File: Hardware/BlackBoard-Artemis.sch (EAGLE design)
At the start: 84 parts, among them IC3 LM1117, J2 CORTEX_DEBUG, J3 POWER_JACKTOE, J5 USB-C, Q1 1.1A/60V/600mΩ, U3 AP2112-3.3V, U4 ARTEMIS_MODULESMD, U5 CH340C, Y1 32.768kHz

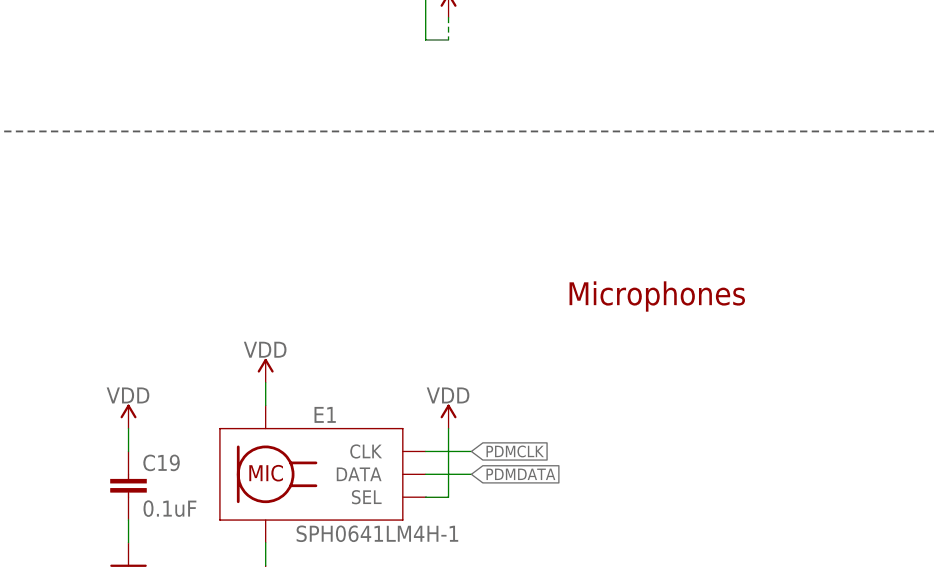
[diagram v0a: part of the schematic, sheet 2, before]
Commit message: Adding production panel
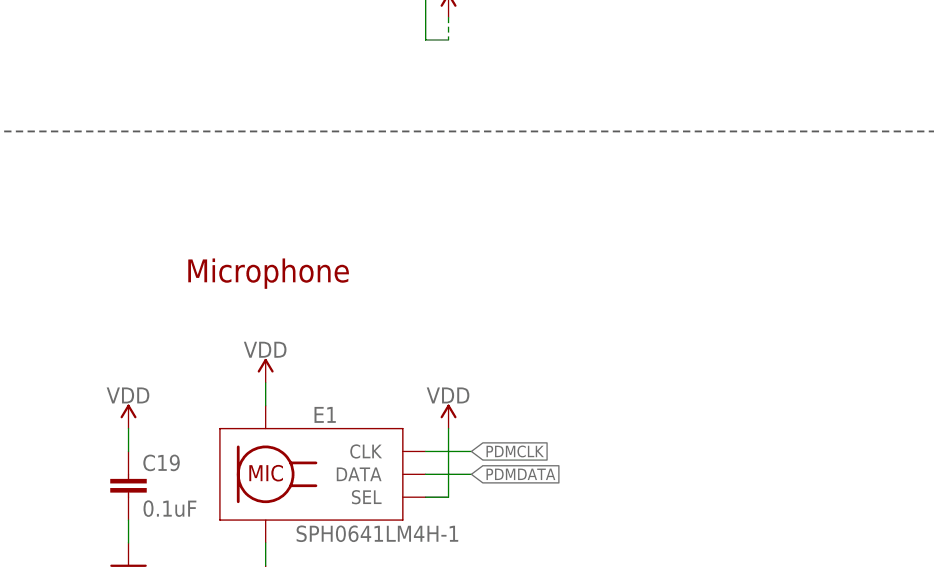
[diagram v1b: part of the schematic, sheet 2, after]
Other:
- note added: "Microphone"
- note removed: "Microphones"
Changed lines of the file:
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@@
 current measurements</text>
 <text x="122.174" y="180.086" size="2.54" layer="94" font="vector" ratio="15" align="center">Power Supplies</text>
-<text x="78.994" y="78.486" size="2.54" layer="94" font="vector" ratio="15" align="center">Microphones</text>
+<text x="35.814" y="81.026" size="2.54" layer="94" font="vector" ratio="15" align="center">Microphone</text>
 <wire x1="0" y1="96.52" x2="147.32" y2="96.52" width="0.2032" layer="97" style="longdash"/>
 <wire x1="147.32" y1="96.52" x2="248.92" y2="96.52" width="0.2032" layer="97" style="longdash"/>

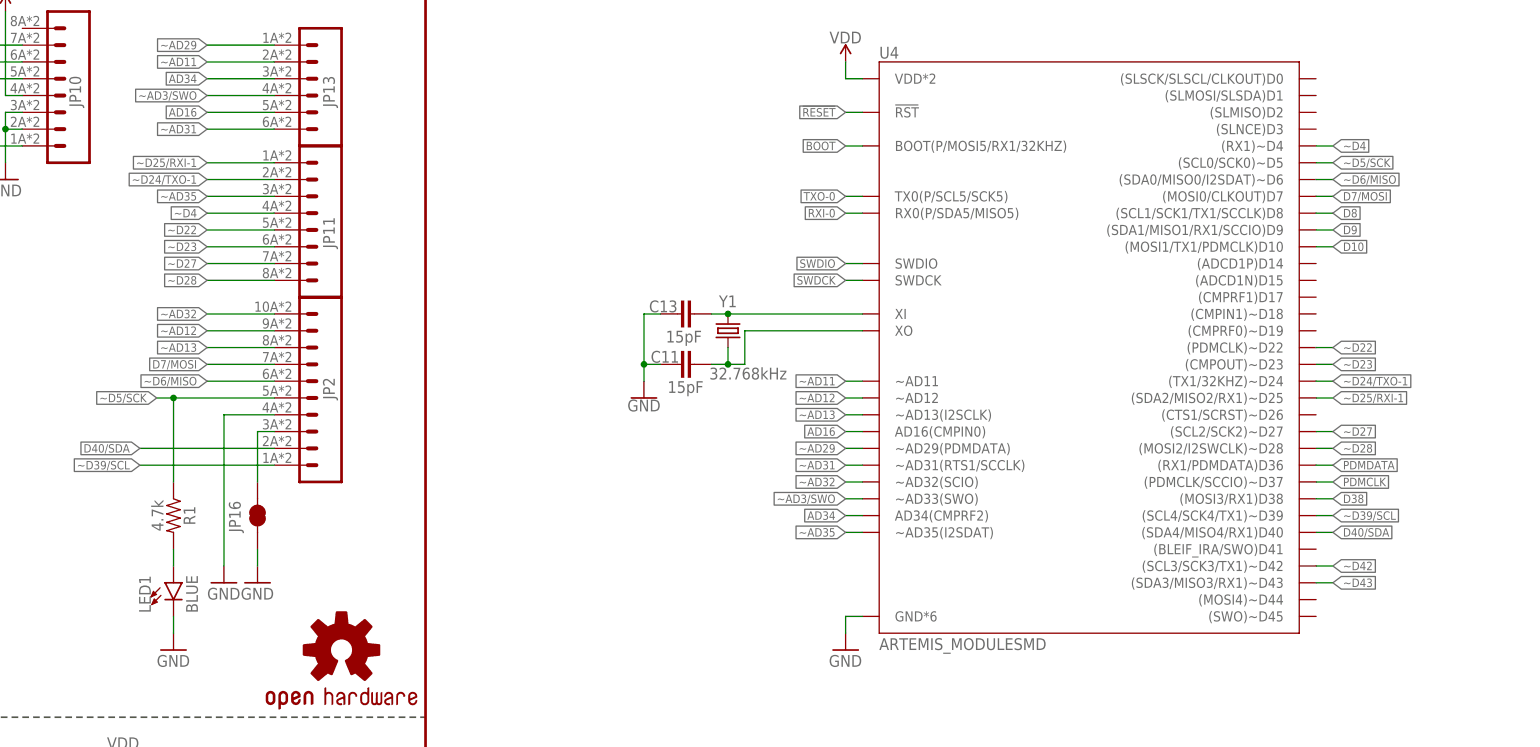
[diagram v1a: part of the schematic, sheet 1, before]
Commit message: Fixing PWM on pin 7
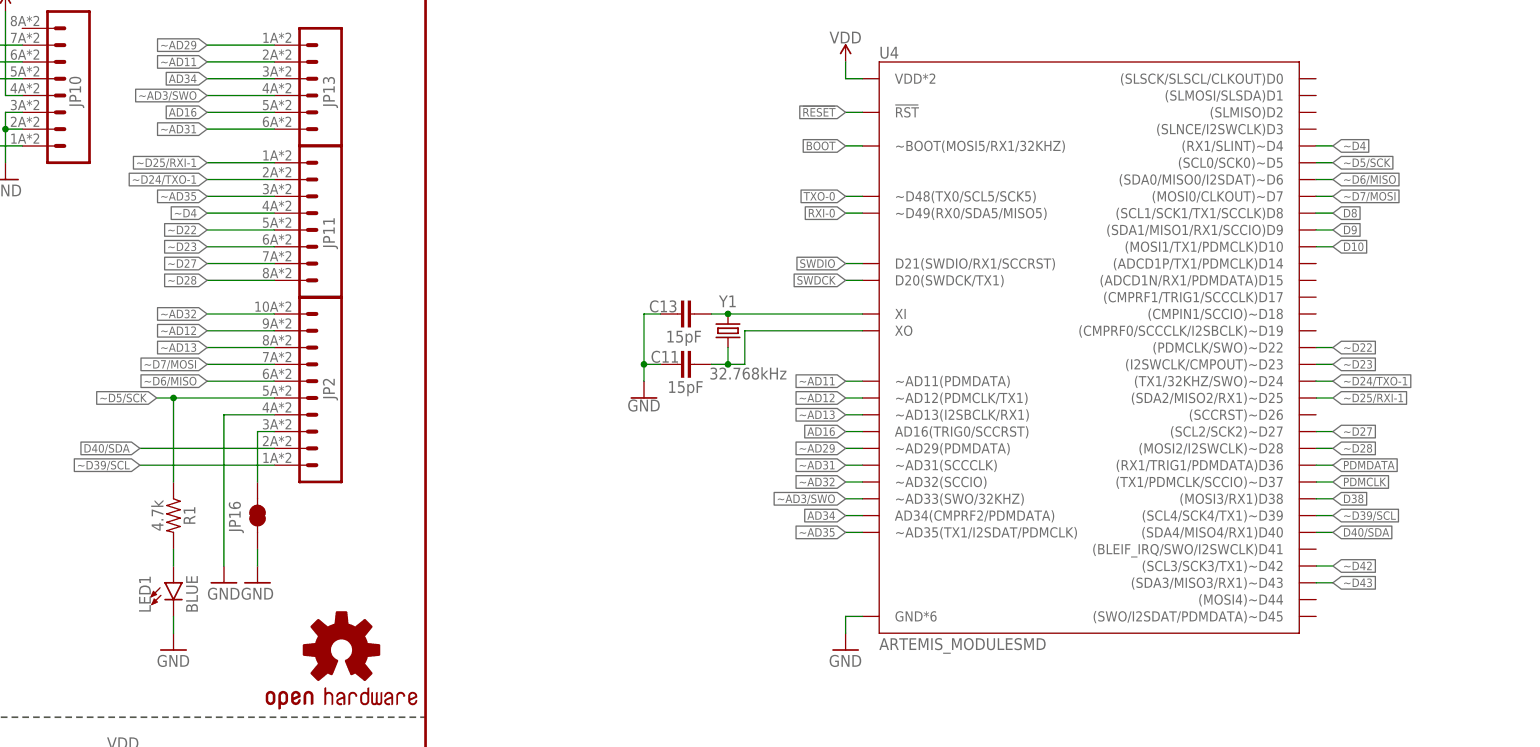
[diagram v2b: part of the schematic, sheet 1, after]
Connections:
- removed net D7/MOSI: JP2.7, U4.(MOSI0/CLKOUT)D7
- new net ~D7/MOSI: JP2.7, U4.(MOSI0/CLKOUT)~D7
- net AD16: now also U4.AD16(TRIG0/SCCRST); no longer U4.AD16(CMPIN0)
- net AD34: now also U4.AD34(CMPRF2/PDMDATA); no longer U4.AD34(CMPRF2)
- net BOOT: now also U4.~BOOT(MOSI5/RX1/32KHZ); no longer U4.BOOT(P/MOSI5/RX1/32KHZ)
- net PDMCLK: now also U4.(TX1/PDMCLK/SCCIO)~D37; no longer U4.(PDMCLK/SCCIO)~D37
- net PDMDATA: now also U4.(RX1/TRIG1/PDMDATA)D36; no longer U4.(RX1/PDMDATA)D36
- net RXI-0: now also U4.~D49(RX0/SDA5/MISO5); no longer U4.RX0(P/SDA5/MISO5)
- net SWDCK: now also U4.D20(SWDCK/TX1); no longer U4.SWDCK
- net SWDIO: now also U4.D21(SWDIO/RX1/SCCRST); no longer U4.SWDIO
- net TXO-0: now also U4.~D48(TX0/SCL5/SCK5); no longer U4.TX0(P/SCL5/SCK5)
- net ~AD11: now also U4.~AD11(PDMDATA); no longer U4.~AD11
- net ~AD12: now also U4.~AD12(PDMCLK/TX1); no longer U4.~AD12
- net ~AD13: now also U4.~AD13(I2SBCLK/RX1); no longer U4.~AD13(I2SCLK)
- net ~AD3/SWO: now also U4.~AD33(SWO/32KHZ); no longer U4.~AD33(SWO)
- net ~AD31: now also U4.~AD31(SCCCLK); no longer U4.~AD31(RTS1/SCCLK)
- net ~AD32: now also U4.~AD32(SCCIO); no longer U4.~AD32(SCIO)
- net ~AD35: now also U4.~AD35(TX1/I2SDAT/PDMCLK); no longer U4.~AD35(I2SDAT)
- net ~D22: now also U4.(PDMCLK/SWO)~D22; no longer U4.(PDMCLK)~D22
- net ~D23: now also U4.(I2SWCLK/CMPOUT)~D23; no longer U4.(CMPOUT)~D23
- net ~D24/TXO-1: now also U4.(TX1/32KHZ/SWO)~D24; no longer U4.(TX1/32KHZ)~D24
- net ~D4: now also U4.(RX1/SLINT)~D4; no longer U4.(RX1)~D4

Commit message: Fix pin 33 silk indicator error
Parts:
- removed U4: ARTEMIS_MODULESMD, Testing:ARTEMIS_MODULESMD
- added U1: ARTEMIS_MODULESMD, Testing:ARTEMIS_MODULESMD
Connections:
- removed net ~AD3/SWO: J2.SWO, JP13.4, U4.~AD33(SWO/32KHZ)
- new net ~AD33/SWO: J2.SWO, JP13.4, U1.~AD33(SWO/32KHZ)
- net !RESET: now also U1.!RST; no longer U4.!RST
- net AD16: now also U1.AD16(TRIG0/SCCRST); no longer U4.AD16(TRIG0/SCCRST)
- net AD34: now also U1.AD34(CMPRF2/PDMDATA); no longer U4.AD34(CMPRF2/PDMDATA)
- net BOOT: now also U1.~BOOT(MOSI5/RX1/32KHZ); no longer U4.~BOOT(MOSI5/RX1/32KHZ)
- net D10: now also U1.(MOSI1/TX1/PDMCLK)D10; no longer U4.(MOSI1/TX1/PDMCLK)D10
- net D38: now also U1.(MOSI3/RX1)D38; no longer U4.(MOSI3/RX1)D38
- net D40/SDA: now also U1.(SDA4/MISO4/RX1)D40; no longer U4.(SDA4/MISO4/RX1)D40
- net D8: now also U1.(SCL1/SCK1/TX1/SCCLK)D8; no longer U4.(SCL1/SCK1/TX1/SCCLK)D8
- net D9: now also U1.(SDA1/MISO1/RX1/SCCIO)D9; no longer U4.(SDA1/MISO1/RX1/SCCIO)D9
- net GND: now also U1.GND*6; no longer U4.GND*6
- net N$7: now also U1.XO; no longer U4.XO
- net N$8: now also U1.XI; no longer U4.XI
- net PDMCLK: now also U1.(TX1/PDMCLK/SCCIO)~D37; no longer U4.(TX1/PDMCLK/SCCIO)~D37
- net PDMDATA: now also U1.(RX1/TRIG1/PDMDATA)D36; no longer U4.(RX1/TRIG1/PDMDATA)D36
- net RXI-0: now also U1.~D49(RX0/SDA5/MISO5); no longer U4.~D49(RX0/SDA5/MISO5)
- net SWDCK: now also U1.D20(SWDCK/TX1); no longer U4.D20(SWDCK/TX1)
- net SWDIO: now also U1.D21(SWDIO/RX1/SCCRST); no longer U4.D21(SWDIO/RX1/SCCRST)
- net TXO-0: now also U1.~D48(TX0/SCL5/SCK5); no longer U4.~D48(TX0/SCL5/SCK5)
- net VDD: now also U1.VDD*2; no longer U4.VDD*2
- net ~AD11: now also U1.~AD11(PDMDATA); no longer U4.~AD11(PDMDATA)
- net ~AD12: now also U1.~AD12(PDMCLK/TX1); no longer U4.~AD12(PDMCLK/TX1)
- net ~AD13: now also U1.~AD13(I2SBCLK/RX1); no longer U4.~AD13(I2SBCLK/RX1)
- net ~AD29: now also U1.~AD29(PDMDATA); no longer U4.~AD29(PDMDATA)
- net ~AD31: now also U1.~AD31(SCCCLK); no longer U4.~AD31(SCCCLK)
- net ~AD32: now also U1.~AD32(SCCIO); no longer U4.~AD32(SCCIO)
- net ~AD35: now also U1.~AD35(TX1/I2SDAT/PDMCLK); no longer U4.~AD35(TX1/I2SDAT/PDMCLK)
- net ~D22: now also U1.(PDMCLK/SWO)~D22; no longer U4.(PDMCLK/SWO)~D22
- net ~D23: now also U1.(I2SWCLK/CMPOUT)~D23; no longer U4.(I2SWCLK/CMPOUT)~D23
- net ~D24/TXO-1: now also U1.(TX1/32KHZ/SWO)~D24; no longer U4.(TX1/32KHZ/SWO)~D24
- net ~D25/RXI-1: now also U1.(SDA2/MISO2/RX1)~D25; no longer U4.(SDA2/MISO2/RX1)~D25
- net ~D27: now also U1.(SCL2/SCK2)~D27; no longer U4.(SCL2/SCK2)~D27
- net ~D28: now also U1.(MOSI2/I2SWCLK)~D28; no longer U4.(MOSI2/I2SWCLK)~D28
- net ~D39/SCL: now also U1.(SCL4/SCK4/TX1)~D39; no longer U4.(SCL4/SCK4/TX1)~D39
- net ~D4: now also U1.(RX1/SLINT)~D4; no longer U4.(RX1/SLINT)~D4
- net ~D42: now also U1.(SCL3/SCK3/TX1)~D42; no longer U4.(SCL3/SCK3/TX1)~D42
- net ~D43: now also U1.(SDA3/MISO3/RX1)~D43; no longer U4.(SDA3/MISO3/RX1)~D43
- net ~D5/SCK: now also U1.(SCL0/SCK0)~D5; no longer U4.(SCL0/SCK0)~D5
- net ~D6/MISO: now also U1.(SDA0/MISO0/I2SDAT)~D6; no longer U4.(SDA0/MISO0/I2SDAT)~D6
- net ~D7/MOSI: now also U1.(MOSI0/CLKOUT)~D7; no longer U4.(MOSI0/CLKOUT)~D7
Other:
- note added: "Optional Bus Masters broken out to SMD pads"
- moved on the sheet: C11, C13, TP11, TP12, TP13, TP14, TP8, TP9, Y1

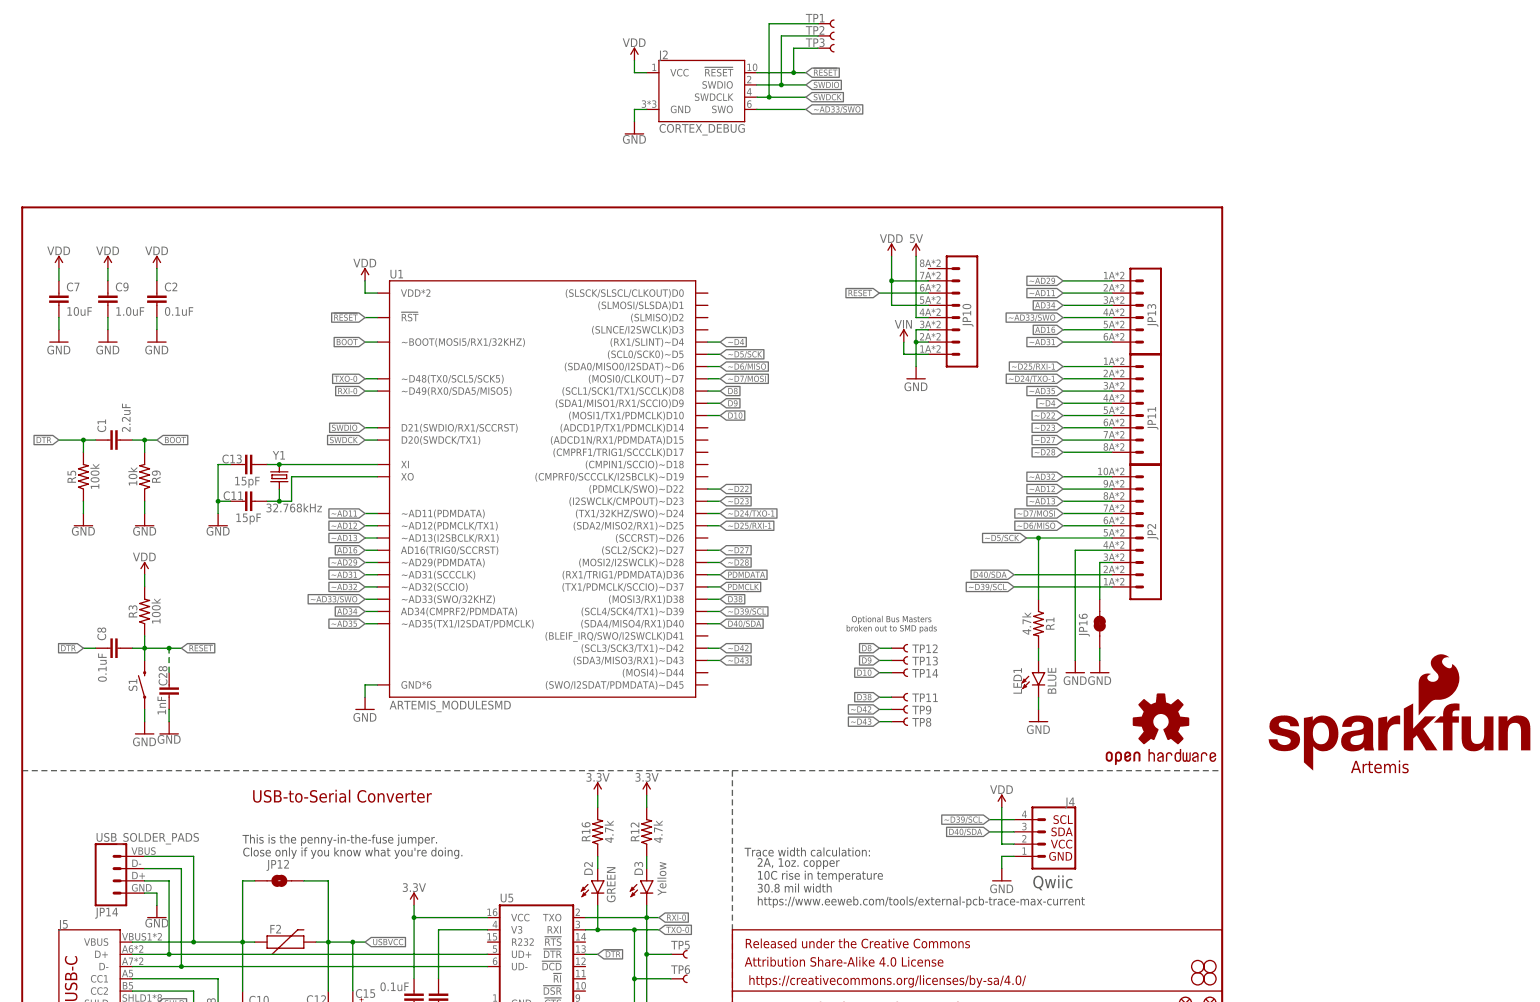
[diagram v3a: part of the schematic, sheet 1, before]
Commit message: Change labels to match variant.
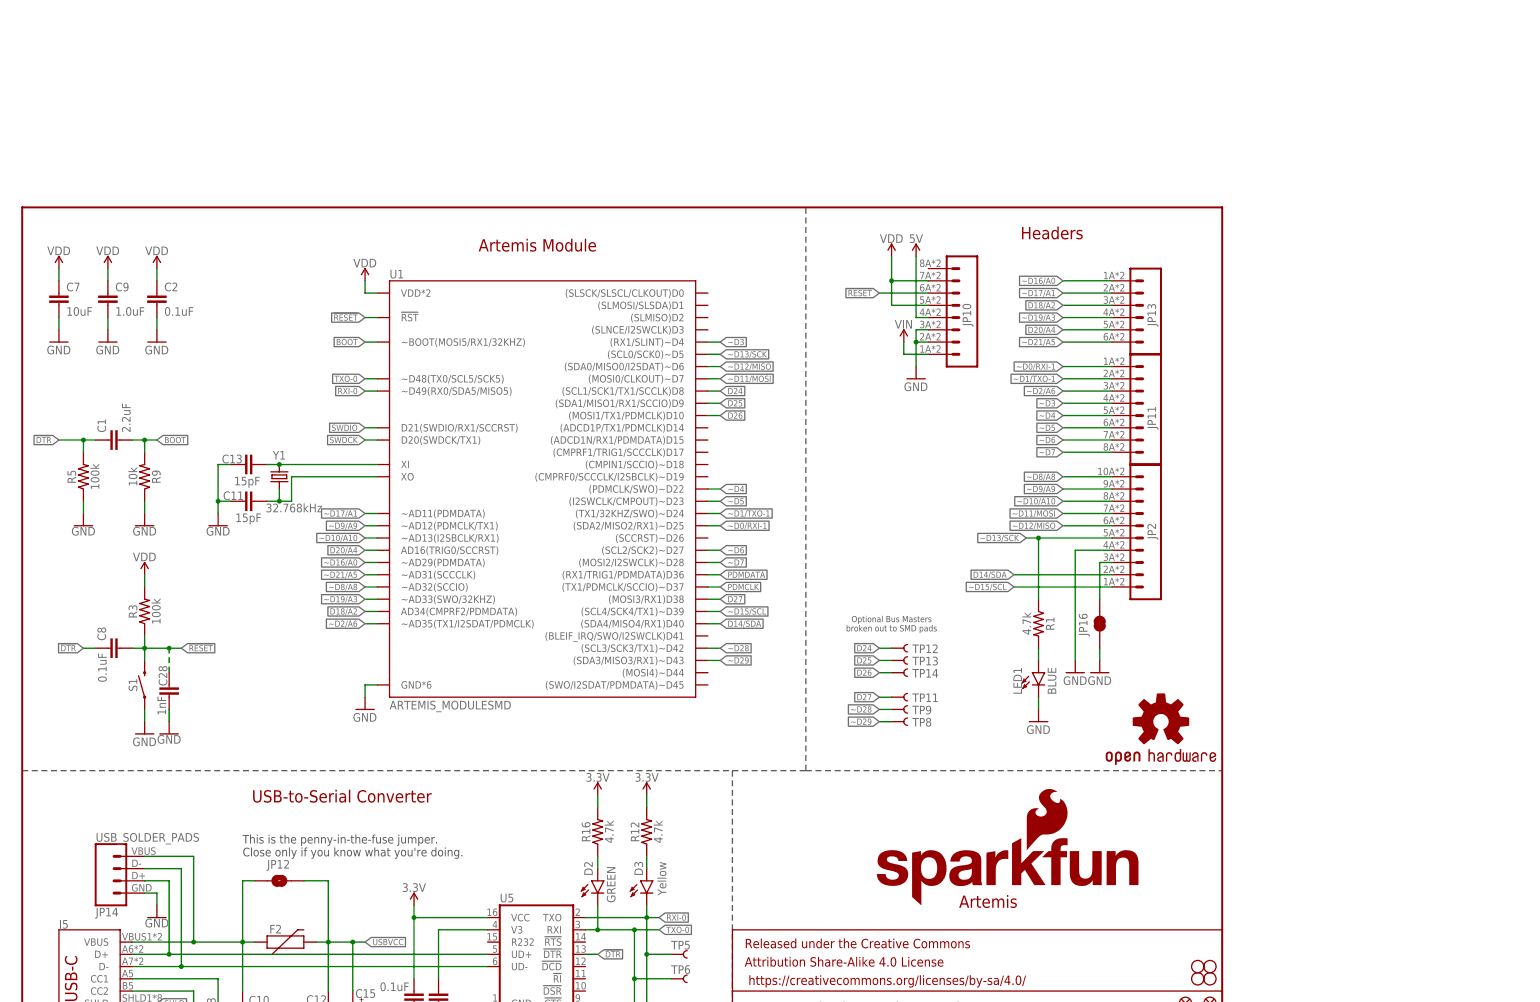
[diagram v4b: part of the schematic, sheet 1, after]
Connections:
- net AD16 renamed D20/A4
- net AD34 renamed D18/A2
- net D10 renamed D26
- net D38 renamed D27
- net D40/SDA renamed D14/SDA
- net D8 renamed D24
- net D9 renamed D25
- net ~AD11 renamed ~D17/A1
- net ~AD12 renamed ~D9/A9
- net ~AD13 renamed ~D10/A10
- net ~AD29 renamed ~D16/A0
- net ~AD31 renamed ~D21/A5
- net ~AD32 renamed ~D8/A8
- net ~AD33/SWO renamed ~D19/A3
- net ~AD35 renamed ~D2/A6
- net ~D23 renamed ~D5
- net ~D24/TXO-1 renamed ~D1/TXO-1
- net ~D25/RXI-1 renamed ~D0/RXI-1
- net ~D27 renamed ~D6
- net ~D39/SCL renamed ~D15/SCL
- net ~D43 renamed ~D29
- net ~D5/SCK renamed ~D13/SCK
- net ~D6/MISO renamed ~D12/MISO
- net ~D7/MOSI renamed ~D11/MOSI
- removed net ~D22: JP11.5, U1.(PDMCLK/SWO)~D22
- removed net ~D42: TP9.1, U1.(SCL3/SCK3/TX1)~D42
- new net ~D3: JP11.4, U1.(RX1/SLINT)~D4
- new net ~D7: JP11.8, U1.(MOSI2/I2SWCLK)~D28
- net ~D28: now also TP9.1, U1.(SCL3/SCK3/TX1)~D42; no longer JP11.8, U1.(MOSI2/I2SWCLK)~D28
- net ~D4: now also JP11.5, U1.(PDMCLK/SWO)~D22; no longer JP11.4, U1.(RX1/SLINT)~D4
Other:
- note added: "Artemis Module"
- note added: "Headers"
- note added: "JTAG"
- note added: "Power"
- moved on the sheet: C19, E1

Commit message: Bump version
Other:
- note added: "X03"
- note removed: "X02"
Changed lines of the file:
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@@
 <text x="66.294" y="63.246" size="2.54" layer="94" font="vector" ratio="15" align="center">USB-to-Serial Converter</text>
 <text x="170.434" y="11.176" size="2.54" layer="94" font="vector">N. Seidle</text>
-<text x="238.76" y="7.62" size="2.54" layer="94" font="vector">X02</text>
+<text x="238.76" y="7.62" size="2.54" layer="94" font="vector">X03</text>
 <wire x1="147.32" y1="68.58" x2="162.56" y2="68.58" width="0.254" layer="97" style="longdash"/>
 <wire x1="162.56" y1="68.58" x2="248.92" y2="68.58" width="0.2032" layer="97" style="longdash"/>
